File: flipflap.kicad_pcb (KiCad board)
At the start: 2 copper layers, 66 x 73.4 mm, 33 parts, among them J1 Conn_01x03, J2 Conn_01x02, U1 TPIC6C595DR, U2 TPIC6C595DR, U3 TPIC6C595DR, U4 74LV165AD, U5 D1 mini, X1 WSL20G, X10 Conn_01x03, X2 WSL20G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

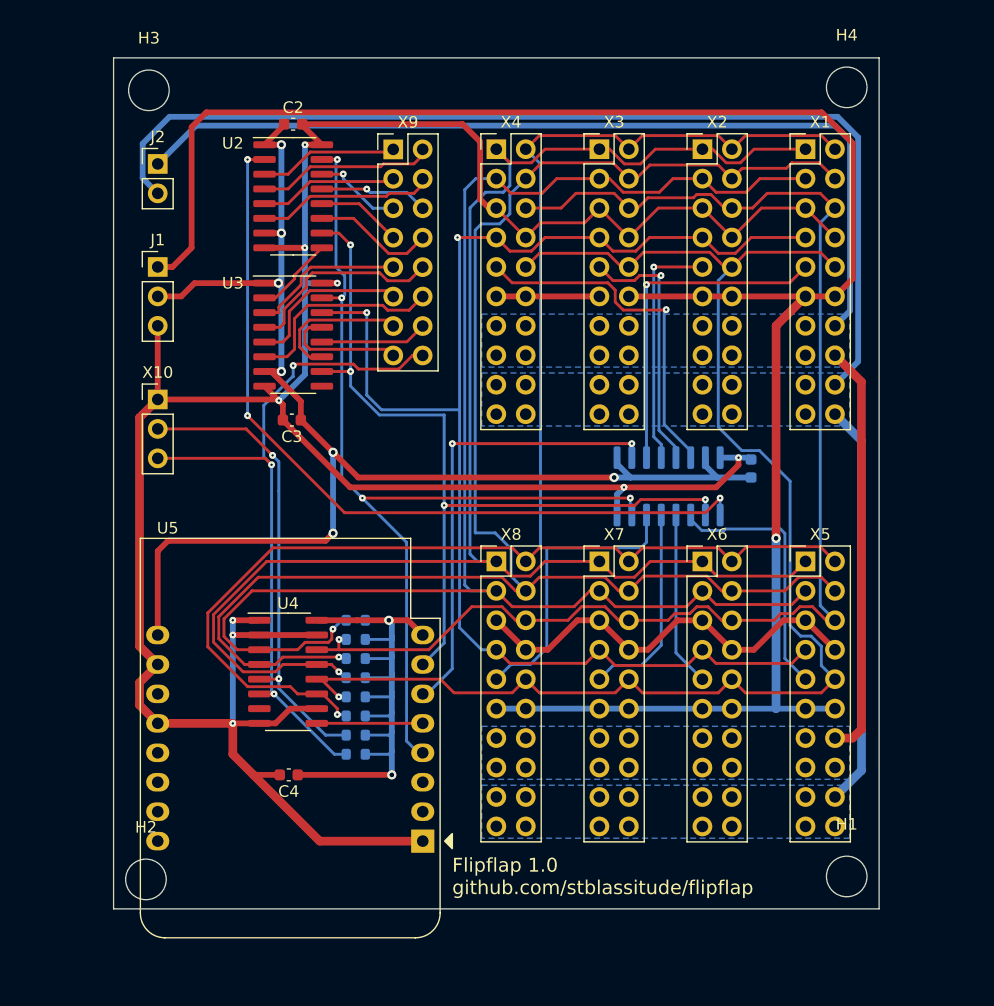
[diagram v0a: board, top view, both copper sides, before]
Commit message: Complete PCB with components only on one side, some corrections included
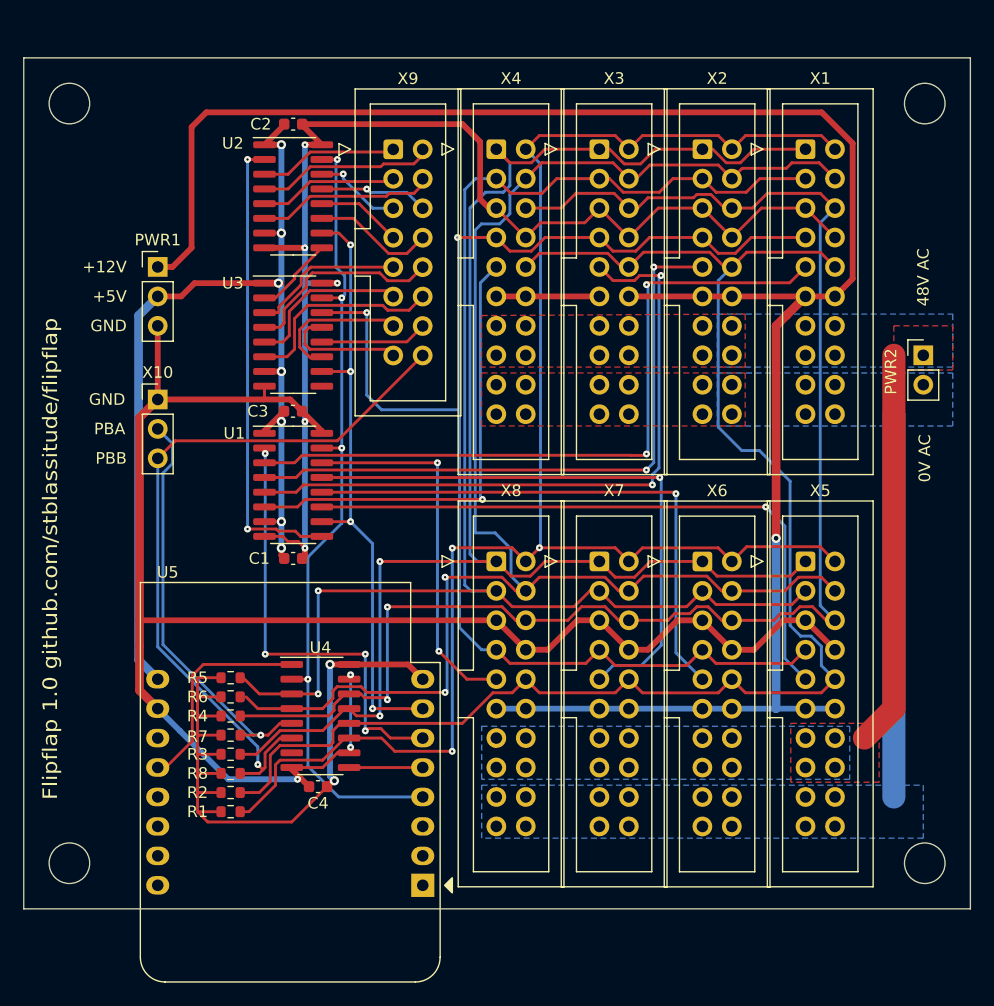
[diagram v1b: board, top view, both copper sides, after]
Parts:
- C1, R1, R2, R3, R4, R5, R6, R7, R8, U1: moved to F.Cu
- X1, X2, X3, X4, X5, X6, X7, X8: footprint Connector_PinHeader_2.54mm:PinHeader_2x10_P2.54mm_Vertical -> Connector_IDC:IDC-Header_2x10_P2.54mm_Vertical
- X9: footprint Connector_PinHeader_2.54mm:PinHeader_2x08_P2.54mm_Vertical -> Connector_IDC:IDC-Header_2x08_P2.54mm_Vertical
- moved PWR2 68.1 mm to (137.2, 30.5)
- moved C1 40.3 mm to (82.8, 48.0), turned to 0 degrees
- moved U1 32.4 mm to (82.8, 41.7), turned to 0 degrees
- moved R1 13.6 mm to (77.4, 69.8), turned to 180 degrees
- moved R2 13.6 mm to (77.4, 68.2), turned to 180 degrees
- moved R3 12.7 mm to (77.4, 64.9), turned to 180 degrees
- moved R4 12.7 mm to (77.4, 61.6), turned to 180 degrees
- moved R5 11.9 mm to (77.4, 58.3), turned to 180 degrees
- moved R6 11.3 mm to (77.4, 59.9), turned to 180 degrees
- moved R8 10.9 mm to (77.4, 66.5), turned to 180 degrees
- moved R7 10.8 mm to (77.4, 63.2), turned to 180 degrees
- moved H3 6.95 mm to (63.5, 8.76)
- moved H4 6.87 mm to (137.3, 8.76)
- moved H1 6.83 mm to (137.3, 74.3)
- moved H2 6.75 mm to (63.5, 74.3)
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- renumbered J1 to PWR1, J2 to PWR2
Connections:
- U4 pad 1: GNDD -> /CS1
- U4 pad 2: GNDD -> /SCK
- U5 pad 1: GNDD -> unconnected-(U5-Pad1)
- U5 pad 12: GNDD -> /CS1
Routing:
- net 0VAC: track 125.3 -> 33.0 mm
- net 48VAC: track 113.9 -> 34.1 mm
- net //ADL2: track 22.4 -> 58.1 mm, vias 1 -> 2
- net //ADL1: track 20.9 -> 55.2 mm, vias 1 -> 2
- net //ADL0: track 29.3 -> 62.3 mm, vias 1 -> 2
- net //ADL6: track 17.8 -> 50.2 mm, vias 0 -> 1
- net //ADL5: track 15.1 -> 47.5 mm, vias 0 -> 1
- net //ADL4: track 22.4 -> 54.6 mm, vias 0 -> 1
- net /S12: track 69.8 -> 40.0 mm, vias 3 -> 2
- net GNDD: track 287.3 -> 258.0 mm, vias 9 -> 8
- net +5V: track 118.7 -> 92.4 mm
- net /CS0: track 73.0 -> 53.0 mm
- net /CS1: track 0.00 -> 18.6 mm
- net //DATA3: track 117.5 -> 130.2 mm, vias 1 -> 2
- net /SCK: track 82.4 -> 71.2 mm
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- added copper zone on F.Cu, net 0VAC
- added copper zone on F.Cu, net 48VAC
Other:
- board size 66 x 73.4 mm -> 81.7 x 73.4 mm
- board text added: "+12V"
- board text added: "+5V"
- board text added: "0V AC"
- board text added: "48V AC"
- board text added: "GND"
- board text added: "PBA"
- board text added: "PBB"

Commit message: As ordered from JLCPCB
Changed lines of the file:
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@@
       (drillshape 0)
       (scaleselection 1)
-      (outputdirectory "fabrication/")
+      (outputdirectory "flipflap-fab/")
     )
   )
@@
     (fp_line (start -3.18 22.88) (end -3.18 -4.1) (layer "F.Fab") (width 0.1))
     (fp_line (start -1.98 6.84) (end -1.98 -3.91) (layer "F.Fab") (width 0.1))
-    (pad "1" thru_hole roundrect (at 0 0) (size 1.7 1.7) (drill 1) (layers *.Cu *.Mask) (roundrect_rratio 0.147059)
+    (pad "1" thru_hole roundrect (at 0 0) (size 1.7 1.7) (drill 1) (layers *.Cu *.Mask) (roundrect_rratio 0.1470588235)
       (net 26 "/{slash}ADC0") (pinfunction "Pin_1") (pintype "passive"))
     (pad "2" thru_hole circle (at 2.54 0) (size 1.7 1.7) (drill 1) (layers *.Cu *.Mask)
@@
     (fp_line (start -3.18 9.38) (end -1.98 9.38) (layer "F.Fab") (width 0.1))
     (fp_line (start 4.52 -3.91) (end 4.52 26.77) (layer "F.Fab") (width 0.1))
-    (pad "1" thru_hole roundrect (at 0 0) (size 1.7 1.7) (drill 1) (layers *.Cu *.Mask) (roundrect_rratio 0.147059)
+    (pad "1" thru_hole roundrect (at 0 0) (size 1.7 1.7) (drill 1) (layers *.Cu *.Mask) (roundrect_rratio 0.1470588235)
       (net 8 "/{slash}DATA2") (pinfunction "Pin_1") (pintype "passive"))
     (pad "2" thru_hole circle (at 2.54 0) (size 1.7 1.7) (drill 1) (layers *.Cu *.Mask)
@@
     (fp_line (start 5.72 27.96) (end -3.18 27.96) (layer "F.Fab") (width 0.1))
     (fp_line (start -3.18 -4.1) (end -2.18 -5.1) (layer "F.Fab") (width 0.1))
-    (pad "1" thru_hole roundrect (at 0 0) (size 1.7 1.7) (drill 1) (layers *.Cu *.Mask) (roundrect_rratio 0.147059)
+    (pad "1" thru_hole roundrect (at 0 0) (size 1.7 1.7) (drill 1) (layers *.Cu *.Mask) (roundrect_rratio 0.1470588235)
       (net 8 "/{slash}DATA2") (pinfunction "Pin_1") (pintype "passive"))
     (pad "2" thru_hole circle (at 2.54 0) (size 1.7 1.7) (drill 1) (layers *.Cu *.Mask)
@@
     (fp_line (start -1.98 -3.91) (end 4.52 -3.91) (layer "F.Fab") (width 0.1))
     (fp_line (start -1.98 13.48) (end -3.18 13.48) (layer "F.Fab") (width 0.1))
-    (pad "1" thru_hole roundrect (at 0 0) (size 1.7 1.7) (drill 1) (layers *.Cu *.Mask) (roundrect_rratio 0.147059)
+    (pad "1" thru_hole roundrect (at 0 0) (size 1.7 1.7) (drill 1) (layers *.Cu *.Mask) (roundrect_rratio 0.1470588235)
       (net 8 "/{slash}DATA2") (pinfunction "Pin_1") (pintype "passive"))
     (pad "2" thru_hole circle (at 2.54 0) (size 1.7 1.7) (drill 1) (layers *.Cu *.Mask)
@@
     (fp_line (start -1.98 13.48) (end -3.18 13.48) (layer "F.Fab") (width 0.1))
     (fp_line (start -3.18 -4.1) (end -2.18 -5.1) (layer "F.Fab") (width 0.1))
-    (pad "1" thru_hole roundrect (at 0 0) (size 1.7 1.7) (drill 1) (layers *.Cu *.Mask) (roundrect_rratio 0.147059)
+    (pad "1" thru_hole roundrect (at 0 0) (size 1.7 1.7) (drill 1) (layers *.Cu *.Mask) (roundrect_rratio 0.1470588235)
       (net 8 "/{slash}DATA2") (pinfunction "Pin_1") (pintype "passive"))
     (pad "2" thru_hole circle (at 2.54 0) (size 1.7 1.7) (drill 1) (layers *.Cu *.Mask)
@@
     (fp_line (start 4.52 26.77) (end -1.98 26.77) (layer "F.Fab") (width 0.1))
     (fp_line (start 5.72 27.96) (end -3.18 27.96) (layer "F.Fab") (width 0.1))
-    (pad "1" thru_hole roundrect (at 0 0) (size 1.7 1.7) (drill 1) (layers *.Cu *.Mask) (roundrect_rratio 0.147059)
+    (pad "1" thru_hole roundrect (at 0 0) (size 1.7 1.7) (drill 1) (layers *.Cu *.Mask) (roundrect_rratio 0.1470588235)
       (net 8 "/{slash}DATA2") (pinfunction "Pin_1") (pintype "passive"))
     (pad "2" thru_hole circle (at 2.54 0) (size 1.7 1.7) (drill 1) (layers *.Cu *.Mask)
@@
     (fp_line (start 4.52 -3.91) (end 4.52 26.77) (layer "F.Fab") (width 0.1))
     (fp_line (start -1.98 26.77) (end -1.98 13.48) (layer "F.Fab") (width 0.1))
-    (pad "1" thru_hole roundrect (at 0 0) (size 1.7 1.7) (drill 1) (layers *.Cu *.Mask) (roundrect_rratio 0.147059)
+    (pad "1" thru_hole roundrect (at 0 0) (size 1.7 1.7) (drill 1) (layers *.Cu *.Mask) (roundrect_rratio 0.1470588235)
       (net 8 "/{slash}DATA2") (pinfunction "Pin_1") (pintype "passive"))
     (pad "2" thru_hole circle (at 2.54 0) (size 1.7 1.7) (drill 1) (layers *.Cu *.Mask)
@@
     (fp_line (start 4.52 26.77) (end -1.98 26.77) (layer "F.Fab") (width 0.1))
     (fp_line (start -1.98 13.48) (end -3.18 13.48) (layer "F.Fab") (width 0.1))
-    (pad "1" thru_hole roundrect (at 0 0) (size 1.7 1.7) (drill 1) (layers *.Cu *.Mask) (roundrect_rratio 0.147059)
+    (pad "1" thru_hole roundrect (at 0 0) (size 1.7 1.7) (drill 1) (layers *.Cu *.Mask) (roundrect_rratio 0.1470588235)
       (net 8 "/{slash}DATA2") (pinfunction "Pin_1") (pintype "passive"))
     (pad "2" thru_hole circle (at 2.54 0) (size 1.7 1.7) (drill 1) (layers *.Cu *.Mask)
@@
     (fp_line (start 5.72 -5.1) (end 5.72 27.96) (layer "F.Fab") (width 0.1))
     (fp_line (start 5.72 27.96) (end -3.18 27.96) (layer "F.Fab") (width 0.1))
-    (pad "1" thru_hole roundrect (at 0 0) (size 1.7 1.7) (drill 1) (layers *.Cu *.Mask) (roundrect_rratio 0.147059)
+    (pad "1" thru_hole roundrect (at 0 0) (size 1.7 1.7) (drill 1) (layers *.Cu *.Mask) (roundrect_rratio 0.1470588235)
       (net 8 "/{slash}DATA2") (pinfunction "Pin_1") (pintype "passive"))
     (pad "2" thru_hole circle (at 2.54 0) (size 1.7 1.7) (drill 1) (layers *.Cu *.Mask)

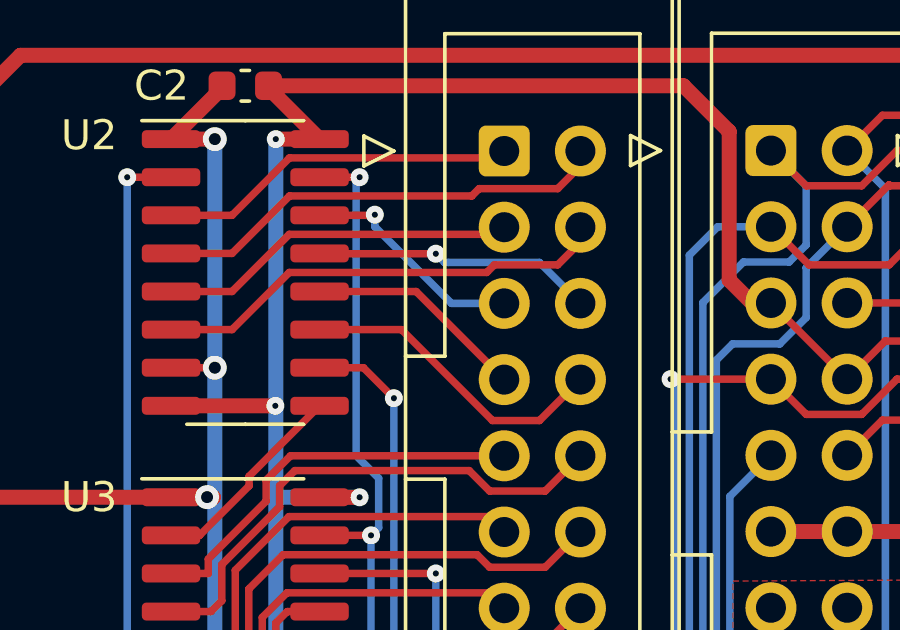
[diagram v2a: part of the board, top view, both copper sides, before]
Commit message: Fix ADC4 to ADC7 (were swapped)
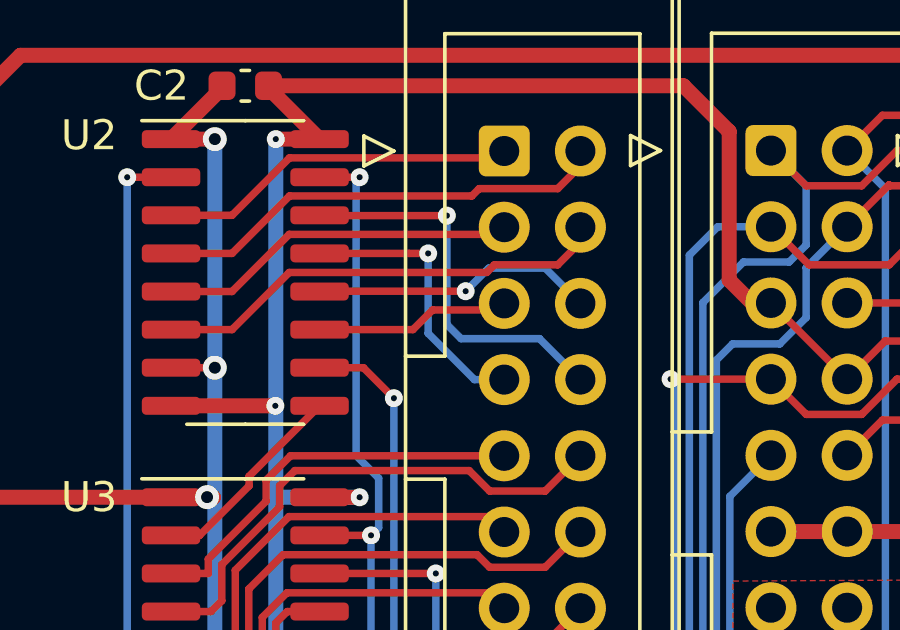
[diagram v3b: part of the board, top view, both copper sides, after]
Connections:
- U2 pad 11: //ADC7 -> //ADC4
- U2 pad 12: //ADC6 -> //ADC5
- U2 pad 13: //ADC5 -> //ADC6
- U2 pad 14: //ADC4 -> //ADC7
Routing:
- net //ADC7: track 10.5 -> 13.1 mm, vias 0 -> 1
- net //ADC6: track 7.37 -> 9.47 mm, vias 0 -> 1
- net //ADC4: track 7.62 -> 6.52 mm, vias 1 -> 0
